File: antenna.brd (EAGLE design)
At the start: 98 x 98 mm, 4 parts, among them X1 BU-SMA-V

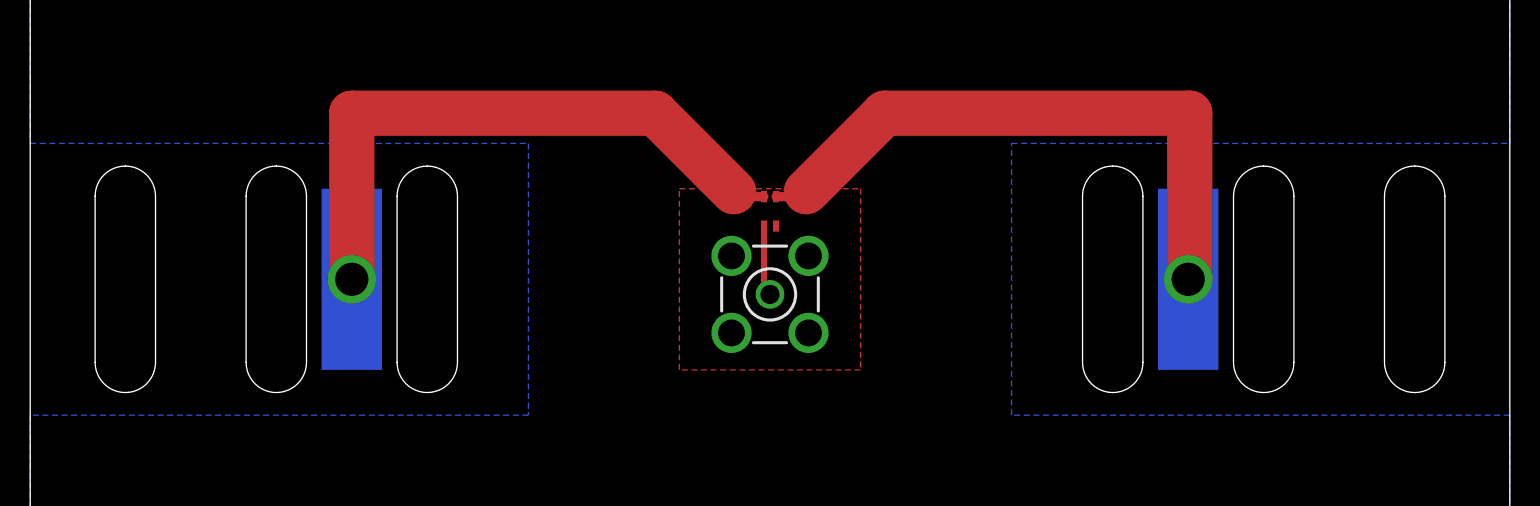
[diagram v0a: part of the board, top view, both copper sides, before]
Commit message: Changed antenna board to 2 cutouts
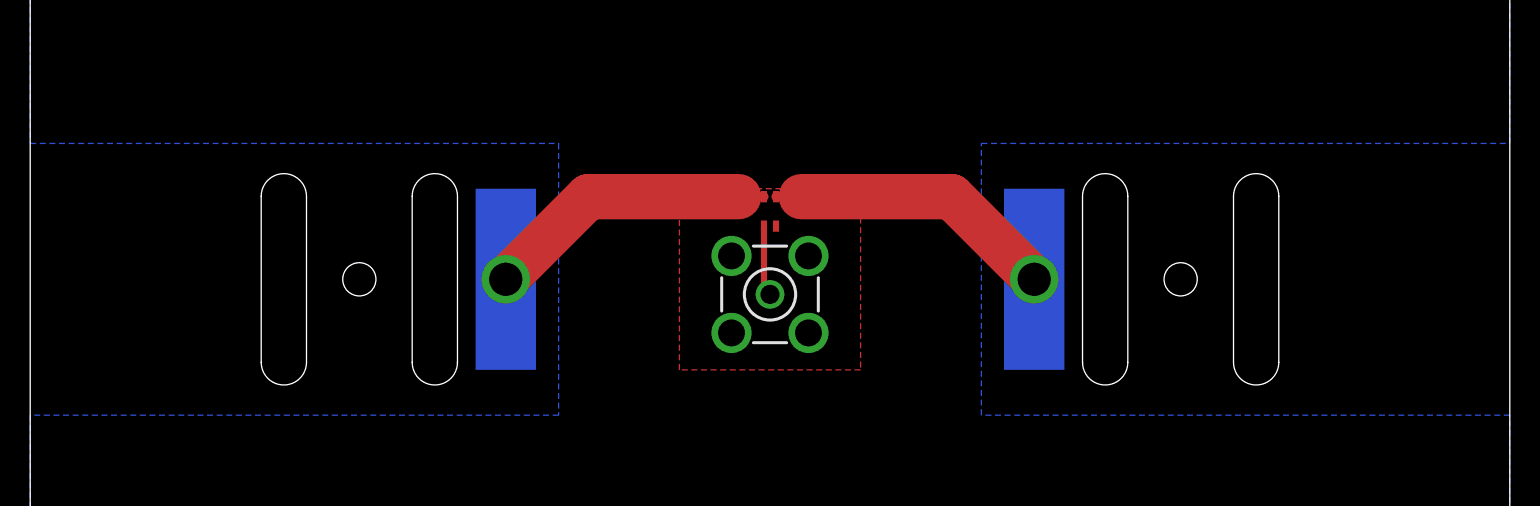
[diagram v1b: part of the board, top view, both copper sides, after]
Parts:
- moved U$2 10.2 mm to (66.5, 49.0)
- moved U$1 10.2 mm to (31.5, 49.0)
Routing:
- net N$3: track 40.8 -> 19.4 mm
- net N$2: track 40.6 -> 19.4 mm
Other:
- outline, holes or cut-outs redrawn
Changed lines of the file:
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@@
 <layer number="43" name="vRestrict" color="2" fill="10" visible="no" active="yes"/>
 <layer number="44" name="Drills" color="7" fill="1" visible="no" active="yes"/>
-<layer number="45" name="Holes" color="7" fill="1" visible="no" active="yes"/>
+<layer number="45" name="Holes" color="7" fill="1" visible="yes" active="yes"/>
 <layer number="46" name="Milling" color="3" fill="1" visible="no" active="yes"/>
 <layer number="47" name="Measures" color="7" fill="1" visible="no" active="yes"/>
@@
 <wire x1="10" y1="88" x2="0" y2="88" width="0" layer="20"/>
 <wire x1="0" y1="88" x2="0" y2="10" width="0" layer="20"/>
-<wire x1="93.7" y1="54.5" x2="93.7" y2="43.5" width="0" layer="20"/>
-<wire x1="93.7" y1="43.5" x2="91.7" y2="41.5" width="0" layer="20" curve="-90"/>
-<wire x1="91.7" y1="41.5" x2="89.7" y2="43.5" width="0" layer="20" curve="-90"/>
-<wire x1="89.7" y1="43.5" x2="89.7" y2="54.5" width="0" layer="20"/>
-<wire x1="89.7" y1="54.5" x2="91.7" y2="56.5" width="0" layer="20" curve="-90"/>
-<wire x1="91.7" y1="56.5" x2="93.7" y2="54.5" width="0" layer="20" curve="-90"/>
-<wire x1="83.7" y1="54.5" x2="83.7" y2="43.5" width="0" layer="20"/>
-<wire x1="83.7" y1="43.5" x2="81.7" y2="41.5" width="0" layer="20" curve="-90"/>
-<wire x1="81.7" y1="41.5" x2="79.7" y2="43.5" width="0" layer="20" curve="-90"/>
+<wire x1="82.7" y1="54.5" x2="82.7" y2="43.5" width="0" layer="20"/>
 <wire x1="79.7" y1="43.5" x2="79.7" y2="54.5" width="0" layer="20"/>
-<wire x1="79.7" y1="54.5" x2="81.7" y2="56.5" width="0" layer="20" curve="-90"/>
-<wire x1="81.7" y1="56.5" x2="83.7" y2="54.5" width="0" layer="20" curve="-90"/>
-<wire x1="73.7" y1="54.5" x2="73.7" y2="43.5" width="0" layer="20"/>
-<wire x1="73.7" y1="43.5" x2="71.7" y2="41.5" width="0" layer="20" curve="-90"/>
-<wire x1="71.7" y1="41.5" x2="69.7" y2="43.5" width="0" layer="20" curve="-90"/>
+<wire x1="72.7" y1="54.5" x2="72.7" y2="43.5" width="0" layer="20"/>
 <wire x1="69.7" y1="43.5" x2="69.7" y2="54.5" width="0" layer="20"/>
-<wire x1="69.7" y1="54.5" x2="71.7" y2="56.5" width="0" layer="20" curve="-90"/>
-<wire x1="71.7" y1="56.5" x2="73.7" y2="54.5" width="0" layer="20" curve="-90"/>
-<wire x1="4.3" y1="43.5" x2="4.3" y2="54.5" width="0" layer="20"/>
-<wire x1="4.3" y1="54.5" x2="6.3" y2="56.5" width="0" layer="20" curve="-90"/>
-<wire x1="6.3" y1="56.5" x2="8.3" y2="54.5" width="0" layer="20" curve="-90"/>
-<wire x1="8.3" y1="54.5" x2="8.3" y2="43.5" width="0" layer="20"/>
-<wire x1="8.3" y1="43.5" x2="6.3" y2="41.5" width="0" layer="20" curve="-90"/>
-<wire x1="6.3" y1="41.5" x2="4.3" y2="43.5" width="0" layer="20" curve="-90"/>
-<wire x1="14.3" y1="43.5" x2="14.3" y2="54.5" width="0" layer="20"/>
-<wire x1="14.3" y1="54.5" x2="16.3" y2="56.5" width="0" layer="20" curve="-90"/>
-<wire x1="16.3" y1="56.5" x2="18.3" y2="54.5" width="0" layer="20" curve="-90"/>
+<wire x1="15.3" y1="43.5" x2="15.3" y2="54.5" width="0" layer="20"/>
 <wire x1="18.3" y1="54.5" x2="18.3" y2="43.5" width="0" layer="20"/>
-<wire x1="18.3" y1="43.5" x2="16.3" y2="41.5" width="0" layer="20" curve="-90"/>
-<wire x1="16.3" y1="41.5" x2="14.3" y2="43.5" width="0" layer="20" curve="-90"/>
-<wire x1="24.3" y1="43.5" x2="24.3" y2="54.5" width="0" layer="20"/>
-<wire x1="24.3" y1="54.5" x2="26.3" y2="56.5" width="0" layer="20" curve="-90"/>
-<wire x1="26.3" y1="56.5" x2="28.3" y2="54.5" width="0" layer="20" curve="-90"/>
+<wire x1="25.3" y1="43.5" x2="25.3" y2="54.5" width="0" layer="20"/>
 <wire x1="28.3" y1="54.5" x2="28.3" y2="43.5" width="0" layer="20"/>
-<wire x1="28.3" y1="43.5" x2="26.3" y2="41.5" width="0" layer="20" curve="-90"/>
-<wire x1="26.3" y1="41.5" x2="24.3" y2="43.5" width="0" layer="20" curve="-90"/>
 <rectangle x1="58.015" y1="20.765" x2="58.055" y2="20.775" layer="200"/>
 <rectangle x1="57.975" y1="20.775" x2="58.115" y2="20.785" layer="200"/>
@@
 <rectangle x1="50.895" y1="66.025" x2="51.025" y2="66.035" layer="201"/>
 <rectangle x1="50.895" y1="66.015" x2="50.965" y2="66.025" layer="201"/>
+<hole x="21.8" y="49" drill="2.2"/>
+<hole x="76.2" y="49" drill="2.2"/>
+<wire x1="15.3" y1="54.5" x2="18.3" y2="54.5" width="0" layer="20" curve="-180" cap="flat"/>
+<wire x1="18.3" y1="43.5" x2="15.3" y2="43.5" width="0" layer="20" curve="-180" cap="flat"/>
+<wire x1="25.3" y1="54.5" x2="28.3" y2="54.5" width="0" layer="20" curve="-180" cap="flat"/>
+<wire x1="28.3" y1="43.5" x2="25.3" y2="43.5" width="0" layer="20" curve="-180" cap="flat"/>
+<wire x1="69.7" y1="54.5" x2="72.7" y2="54.5" width="0" layer="20" curve="-180" cap="flat"/>
+<wire x1="72.7" y1="43.5" x2="69.7" y2="43.5" width="0" layer="20" curve="-180" cap="flat"/>
+<wire x1="79.7" y1="54.5" x2="82.7" y2="54.5" width="0" layer="20" curve="-180" cap="flat"/>
+<wire x1="82.7" y1="43.5" x2="79.7" y2="43.5" width="0" layer="20" curve="-180" cap="flat"/>
 </plain>
 <attributes>
@@
 </element>
 <element name="B1" library="Balun" package="BALUN" value="BALUN" x="49" y="53.5" smashed="yes" rot="R90"/>
-<element name="U$1" library="TapeAntenna" package="TAPEANTENNA" value="TAPEANTENNA" x="21.3" y="49" rot="MR0"/>
-<element name="U$2" library="TapeAntenna" package="TAPEANTENNA" value="TAPEANTENNA" x="76.7" y="49" rot="MR0"/>
+<element name="U$1" library="TapeAntenna" package="TAPEANTENNA" value="TAPEANTENNA" x="31.5" y="49" rot="MR0"/>
+<element name="U$2" library="TapeAntenna" package="TAPEANTENNA" value="TAPEANTENNA" x="66.5" y="49" rot="MR0"/>
 </elements>
 <signals>
@@
 <polygon width="0.4064" layer="16">
 <vertex x="0" y="58"/>
-<vertex x="33" y="58"/>
-<vertex x="33" y="40"/>
+<vertex x="35" y="58"/>
+<vertex x="35" y="40"/>
 <vertex x="0" y="40"/>
 <vertex x="0" y="10"/>
@@
 <vertex x="98" y="10"/>
 <vertex x="98" y="40"/>
-<vertex x="65" y="40"/>
-<vertex x="65" y="58"/>
+<vertex x="63" y="40"/>
+<vertex x="63" y="58"/>
 <vertex x="98" y="58"/>
 <vertex x="98" y="88"/>
@@
 <contactref element="U$1" pad="P$1"/>
 <contactref element="U$1" pad="P$2"/>
-<wire x1="21.3" y1="49" x2="21.3" y2="60" width="3" layer="1"/>
-<wire x1="21.3" y1="60" x2="41.4" y2="60" width="3" layer="1"/>
-<wire x1="41.4" y1="60" x2="46.6" y2="54.8" width="3" layer="1"/>
 <wire x1="48.6" y1="54.475" x2="46.925" y2="54.475" width="0.6096" layer="1"/>
-<wire x1="46.925" y1="54.475" x2="46.6" y2="54.8" width="0.6096" layer="1"/>
+<wire x1="46.925" y1="54.475" x2="36.975" y2="54.475" width="3" layer="1"/>
+<wire x1="36.975" y1="54.475" x2="31.5" y2="49" width="3" layer="1"/>
 </signal>
 <signal name="N$3">
@@
 <contactref element="U$2" pad="P$1"/>
 <contactref element="U$2" pad="P$2"/>
-<wire x1="76.7" y1="49" x2="76.8" y2="49" width="3" layer="1"/>
-<wire x1="76.8" y1="49" x2="76.8" y2="60" width="3" layer="1"/>
-<wire x1="76.8" y1="60" x2="56.6" y2="60" width="3" layer="1"/>
-<wire x1="56.6" y1="60" x2="51.4" y2="54.8" width="3" layer="1"/>
 <wire x1="49.4" y1="54.475" x2="51.075" y2="54.475" width="0.6096" layer="1"/>
-<wire x1="51.075" y1="54.475" x2="51.4" y2="54.8" width="0.6096" layer="1"/>
+<wire x1="51.075" y1="54.475" x2="61.025" y2="54.475" width="3" layer="1"/>
+<wire x1="61.025" y1="54.475" x2="66.5" y2="49" width="3" layer="1"/>
 </signal>
 </signals>

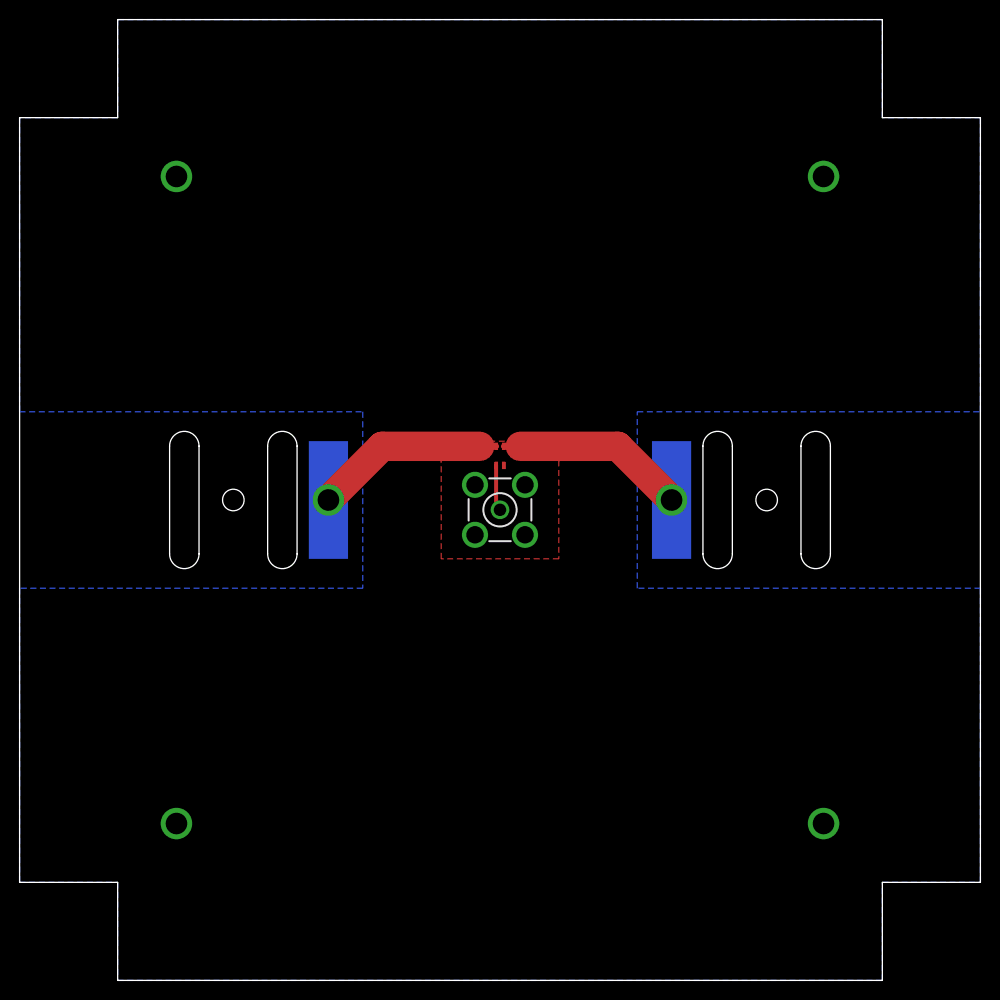
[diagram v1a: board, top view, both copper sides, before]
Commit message: Mitered corners of mainboard
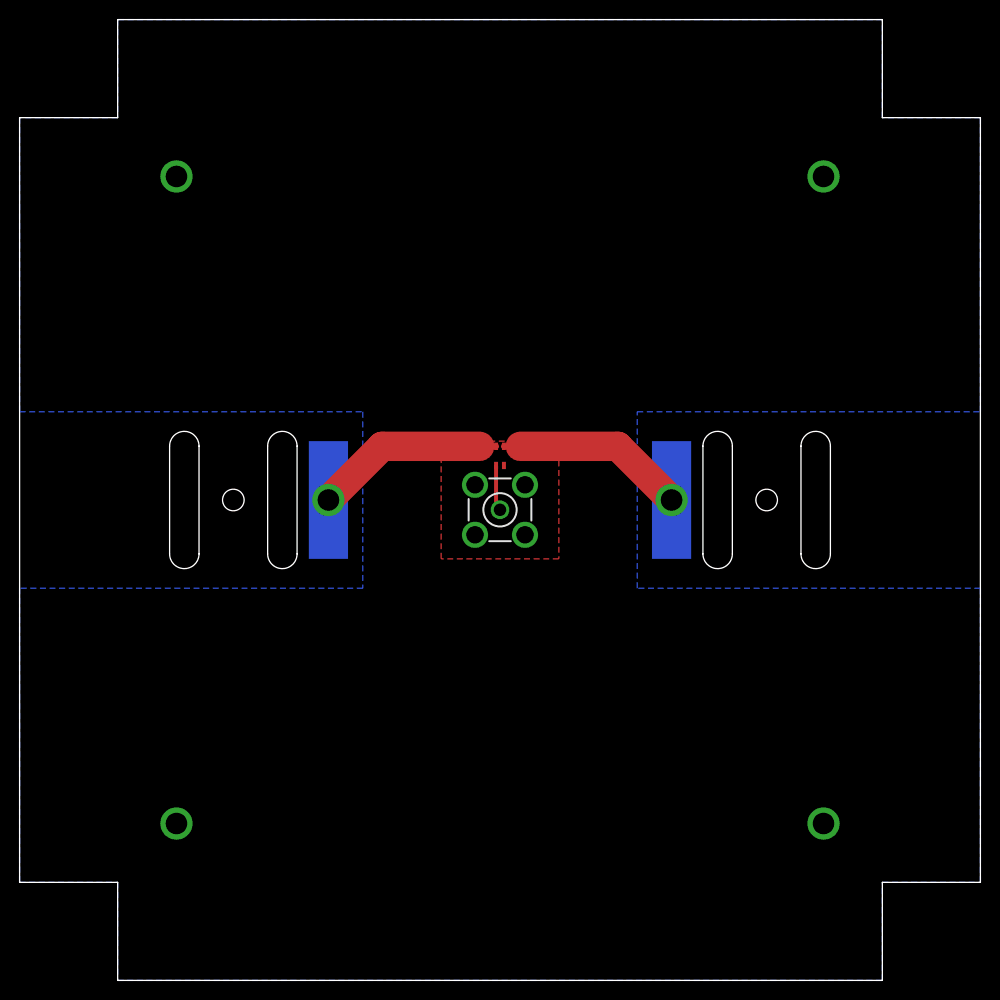
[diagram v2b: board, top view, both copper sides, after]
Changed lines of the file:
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@@
 </class>
 </classes>
-<designrules name="LaenPCBOrder">
-<description language="de">&lt;b&gt;EAGLE Design Rules&lt;/b&gt;
+<designrules name="SSC-EAGLE-2Lyr_v1.0.0.3">
+<description language="en">&lt;b&gt;EAGLE Design Rules for *2* Layer Designs (DS)&lt;/b&gt;
 &lt;p&gt;
-Die Standard-Design-Rules sind so gewählt, dass sie für
-die meisten Anwendungen passen. Sollte ihre Platine
-besondere Anforderungen haben, treffen Sie die erforderlichen
-Einstellungen hier und speichern die Design Rules unter
-einem neuen Namen ab.</description>
-<description language="en">&lt;b&gt;Laen's PCB Order Design Rules&lt;/b&gt;
+This Sunstone Circuits 2 Layer .DRU has been set to cover our minimum requirements for our double sided products. For questions, comments, suggestions, please contact Sunstone Customer Support: &lt;p&gt;&lt;b&gt;Email:&lt;/b&gt;  mailto:support@sunstone.com&lt;br&gt;&lt;b&gt;Phone:&lt;/b&gt; 800-228-8198.&lt;p&gt; v1.1Mod10/16/07~Layers-core reversal.Distance C/D.Restring%.Supply G%.&lt;p&gt; v1.2 Mod12/06/07~Distance C/D to 20mils.&lt;p&gt;v1.3Mod12/12/07~Supply/Annulus Value to 12.5mils&lt;p&gt;1/15/08 SSC-EAGLE-2Lyr_v1.0.0.3~For Release&lt;p&gt;10/3/08 Description Edit.&lt;p&gt;
 &lt;p&gt;
-Please make sure your boards conform to these design rules.</description>
+&lt;i&gt;Attention: Upon running the design check and making modifications, please remember to save any changes before closing the application and sending in your board file to Sunstone Circuits for conversion.&lt;i&gt;</description>
 <param name="layerSetup" value="(1*16)"/>
-<param name="mtCopper" value="0.0356mm 0.0356mm 0.0356mm 0.0356mm 0.0356mm 0.0356mm 0.0356mm 0.0356mm 0.0356mm 0.0356mm 0.0356mm 0.0356mm 0.0356mm 0.0356mm 0.0356mm 0.0356mm"/>
-<param name="mtIsolate" value="1.5011mm 0.1499mm 0.2007mm 0.1499mm 0.2007mm 0.1499mm 0.2007mm 0.1499mm 0.2007mm 0.1499mm 0.2007mm 0.1499mm 0.2007mm 0.1499mm 0.2007mm"/>
+<param name="mtCopper" value="0.0178mm 0.0356mm 0.0356mm 0.0356mm 0.0356mm 0.0356mm 0.0356mm 0.0356mm 0.0356mm 0.0356mm 0.0356mm 0.0356mm 0.0356mm 0.0356mm 0.0356mm 0.0178mm"/>
+<param name="mtIsolate" value="59mil 0.1499mm 0.2007mm 0.1499mm 0.2007mm 0.1499mm 0.2007mm 0.1499mm 0.2007mm 0.1499mm 0.2007mm 0.1499mm 0.2007mm 0.1499mm 0.2007mm"/>
 <param name="mdWireWire" value="6mil"/>
 <param name="mdWirePad" value="6mil"/>
@@
 <param name="mdViaViaSameLayer" value="8mil"/>
 <param name="mnLayersViaInSmd" value="2"/>
-<param name="mdCopperDimension" value="15mil"/>
-<param name="mdDrill" value="6mil"/>
+<param name="mdCopperDimension" value="20mil"/>
+<param name="mdDrill" value="16mil"/>
 <param name="mdSmdStop" value="0mil"/>
 <param name="msWidth" value="6mil"/>
-<param name="msDrill" value="13mil"/>
-<param name="msMicroVia" value="13mil"/>
+<param name="msDrill" value="14mil"/>
+<param name="msMicroVia" value="9.9898mm"/>
 <param name="msBlindViaRatio" value="0.5"/>
 <param name="rvPadTop" value="0.25"/>
@@
 <param name="rvMicroViaOuter" value="0.25"/>
 <param name="rvMicroViaInner" value="0.25"/>
-<param name="rlMinPadTop" value="7mil"/>
-<param name="rlMaxPadTop" value="20mil"/>
-<param name="rlMinPadInner" value="7mil"/>
-<param name="rlMaxPadInner" value="20mil"/>
-<param name="rlMinPadBottom" value="7mil"/>
-<param name="rlMaxPadBottom" value="20mil"/>
-<param name="rlMinViaOuter" value="7mil"/>
-<param name="rlMaxViaOuter" value="20mil"/>
-<param name="rlMinViaInner" value="7mil"/>
-<param name="rlMaxViaInner" value="20mil"/>
-<param name="rlMinMicroViaOuter" value="4mil"/>
-<param name="rlMaxMicroViaOuter" value="20mil"/>
-<param name="rlMinMicroViaInner" value="4mil"/>
-<param name="rlMaxMicroViaInner" value="20mil"/>
+<param name="rlMinPadTop" value="8mil"/>
+<param name="rlMaxPadTop" value="999mil"/>
+<param name="rlMinPadInner" value="0mil"/>
+<param name="rlMaxPadInner" value="0mil"/>
+<param name="rlMinPadBottom" value="8mil"/>
+<param name="rlMaxPadBottom" value="999mil"/>
+<param name="rlMinViaOuter" value="8mil"/>
+<param name="rlMaxViaOuter" value="999mil"/>
+<param name="rlMinViaInner" value="0mil"/>
+<param name="rlMaxViaInner" value="0mil"/>
+<param name="rlMinMicroViaOuter" value="8mil"/>
+<param name="rlMaxMicroViaOuter" value="999mil"/>
+<param name="rlMinMicroViaInner" value="0mil"/>
+<param name="rlMaxMicroViaInner" value="0mil"/>
 <param name="psTop" value="-1"/>
 <param name="psBottom" value="-1"/>
@@
 <param name="checkRestrict" value="1"/>
 <param name="useDiameter" value="13"/>
-<param name="maxErrors" value="50"/>
+<param name="maxErrors" value="500"/>
 </designrules>
 <autorouter>
